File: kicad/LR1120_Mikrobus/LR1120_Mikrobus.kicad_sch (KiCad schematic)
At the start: 8 parts, among them IC1 BGA524N6E6327XTSA1, IC2 SKY13588-460LF, IC3 M24128-BFMH6TG, U1 LR1120, U4 LIS2DE12

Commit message: Small corrections from last commit
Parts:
- added U?: NT2016SA-40M-ENA4203A, symbol TCXO:NT2016SA-40M-ENA4203A
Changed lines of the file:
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@@
     (pin "9")
+  )
+  (symbol (lib_id "TCXO:NT2016SA-40M-ENA4203A") (at 57.15 66.04 0) (unit 1)
+    (in_bom yes) (on_board yes) (fields_autoplaced)
+    (property "Reference" "U?" (id 0) (at 58.42 53.34 0))
+    (property "Value" "NT2016SA-40M-ENA4203A" (id 1) (at 58.42 55.88 0))
+    (property "Footprint" "" (id 2) (at 57.15 66.04 0)
+      (effects (font (size 1.27 1.27)) hide)
+    )
+    (property "Datasheet" "" (id 3) (at 57.15 66.04 0)
+      (effects (font (size 1.27 1.27)) hide)
+    )
+    (pin "1")
+    (pin "2")
+    (pin "3")
+    (pin "4")
   )
   (symbol (lib_id "M24128-BFMH6TG:M24128-BFMH6TG") (at 233.68 85.09 0) (unit 1)
@@
       (reference "U4") (unit 1) (value "LIS2DE12") (footprint "Package_LGA:LGA-12_2x2mm_P0.5mm")
     )
+    (path "/ef4af352-5d7c-4ee8-a333-c7263e32c96e"
+      (reference "U?") (unit 1) (value "NT2016SA-40M-ENA4203A") (footprint "")
+    )
     (path "/30d9f59d-f72b-41c4-8214-d95fedfe532c"

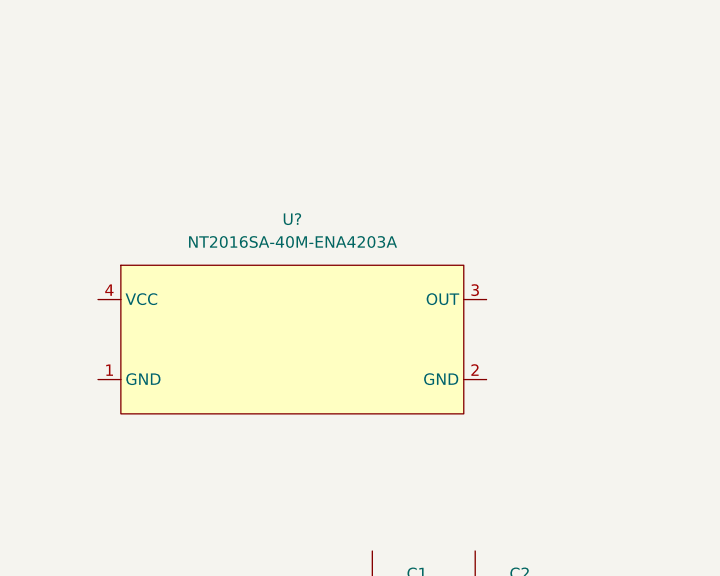
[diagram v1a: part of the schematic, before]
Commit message: tcxo footprint and symbol ready
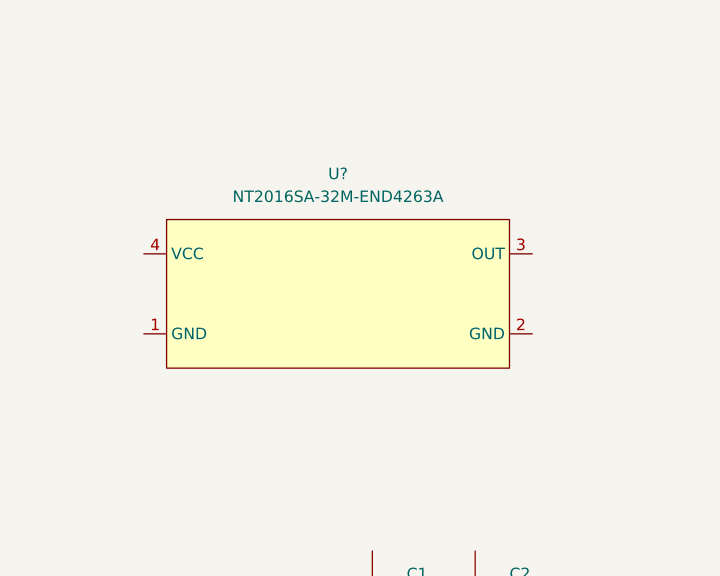
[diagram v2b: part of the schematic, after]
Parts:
- removed U?: NT2016SA-40M-ENA4203A, symbol TCXO:NT2016SA-40M-ENA4203A
- added U?: NT2016SA-32M-END4263A, TXCO:NT2016SA-32M-END4263A, symbol TCXO:NT2016SA-32M-END4263A
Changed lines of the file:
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@@
     (pin "9")
+  )
+  (symbol (lib_id "TCXO:NT2016SA-32M-END4263A") (at 62.23 60.96 0) (unit 1)
+    (in_bom yes) (on_board yes) (fields_autoplaced)
+    (property "Reference" "U?" (id 0) (at 63.5 48.26 0))
+    (property "Value" "NT2016SA-32M-END4263A" (id 1) (at 63.5 50.8 0))
+    (property "Footprint" "TXCO:NT2016SA-32M-END4263A" (id 2) (at 62.23 60.96 0)
+      (effects (font (size 1.27 1.27)) hide)
+    )
+    (property "Datasheet" "" (id 3) (at 62.23 60.96 0)
+      (effects (font (size 1.27 1.27)) hide)
+    )
+    (pin "1")
+    (pin "2")
+    (pin "3")
+    (pin "4")
   )
   (symbol (lib_id "Device:C") (at 67.31 93.98 0) (unit 1)
@@
     (pin "9")
   )
-  (symbol (lib_id "TCXO:NT2016SA-40M-ENA4203A") (at 57.15 66.04 0) (unit 1)
-    (in_bom yes) (on_board yes) (fields_autoplaced)
-    (property "Reference" "U?" (id 0) (at 58.42 53.34 0))
-    (property "Value" "NT2016SA-40M-ENA4203A" (id 1) (at 58.42 55.88 0))
-    (property "Footprint" "" (id 2) (at 57.15 66.04 0)
-      (effects (font (size 1.27 1.27)) hide)
-    )
-    (property "Datasheet" "" (id 3) (at 57.15 66.04 0)
-      (effects (font (size 1.27 1.27)) hide)
-    )
-    (pin "1")
-    (pin "2")
-    (pin "3")
-    (pin "4")
-  )
   (symbol (lib_id "M24128-BFMH6TG:M24128-BFMH6TG") (at 233.68 85.09 0) (unit 1)
     (in_bom yes) (on_board yes) (fields_autoplaced)
@@
       (reference "U4") (unit 1) (value "LIS2DE12") (footprint "Package_LGA:LGA-12_2x2mm_P0.5mm")
     )
-    (path "/ef4af352-5d7c-4ee8-a333-c7263e32c96e"
-      (reference "U?") (unit 1) (value "NT2016SA-40M-ENA4203A") (footprint "")
+    (path "/82107e2f-5ae3-45c6-a719-55de61f5c3b5"
+      (reference "U?") (unit 1) (value "NT2016SA-32M-END4263A") (footprint "TXCO:NT2016SA-32M-END4263A")
     )
     (path "/30d9f59d-f72b-41c4-8214-d95fedfe532c"

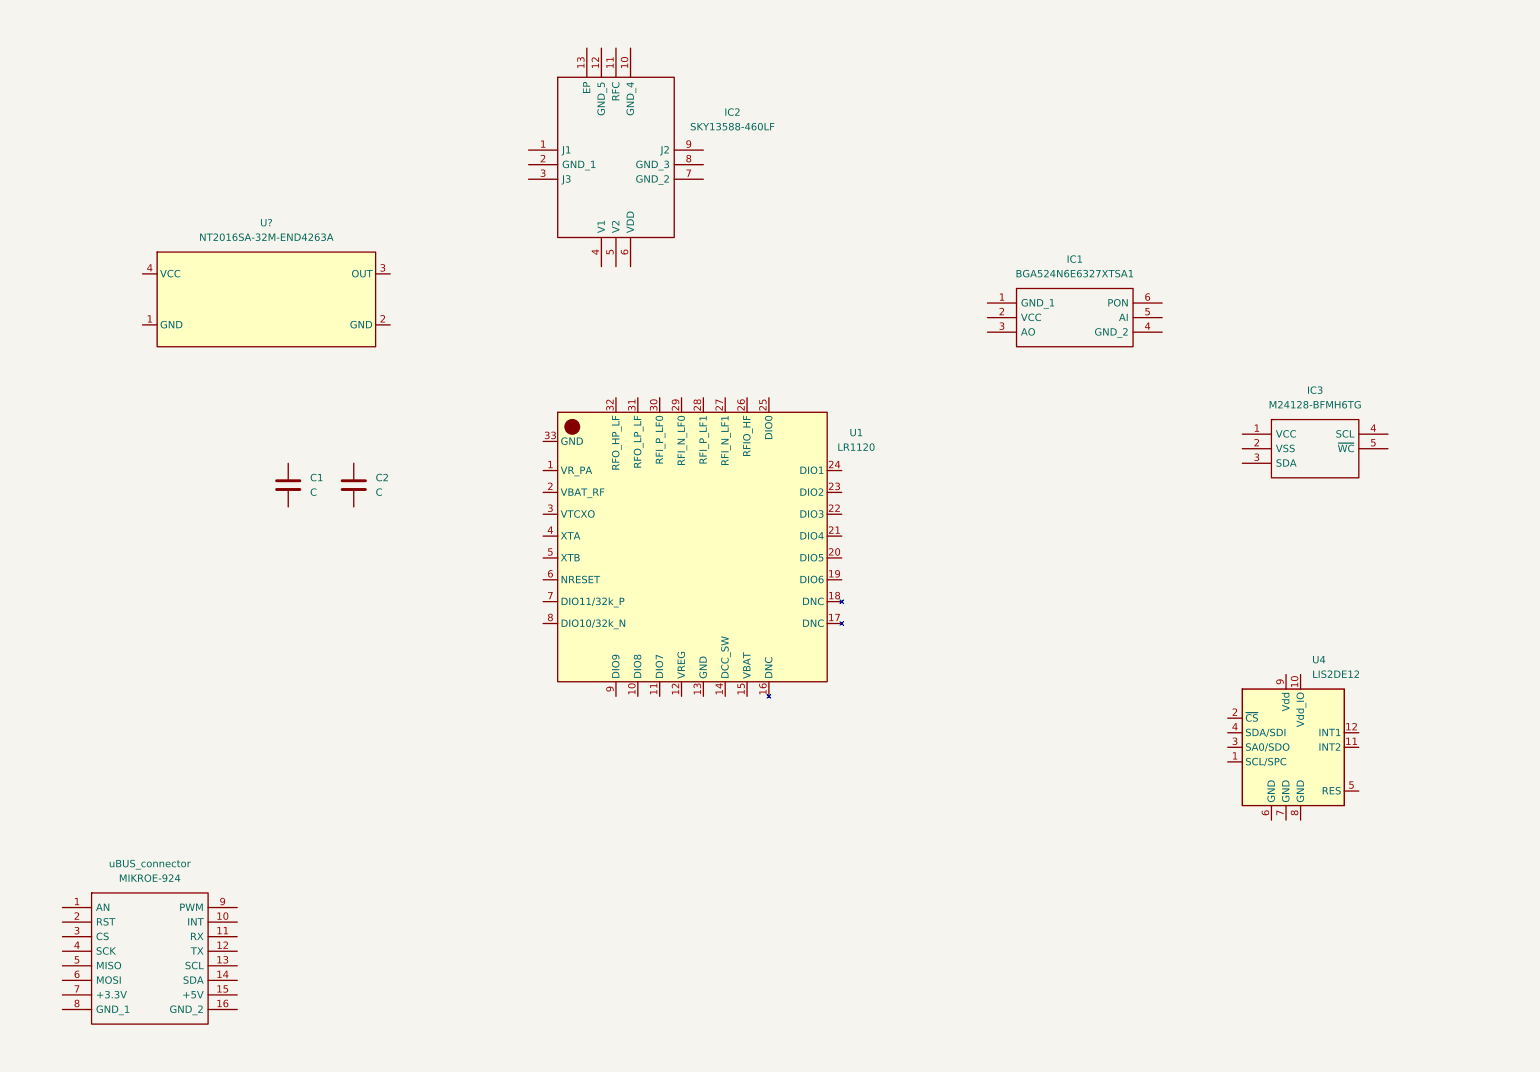
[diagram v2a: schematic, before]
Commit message: Q2 and Q3 placed
downloaded Q2 symbol and footprint. created Q3 symbol and footprint
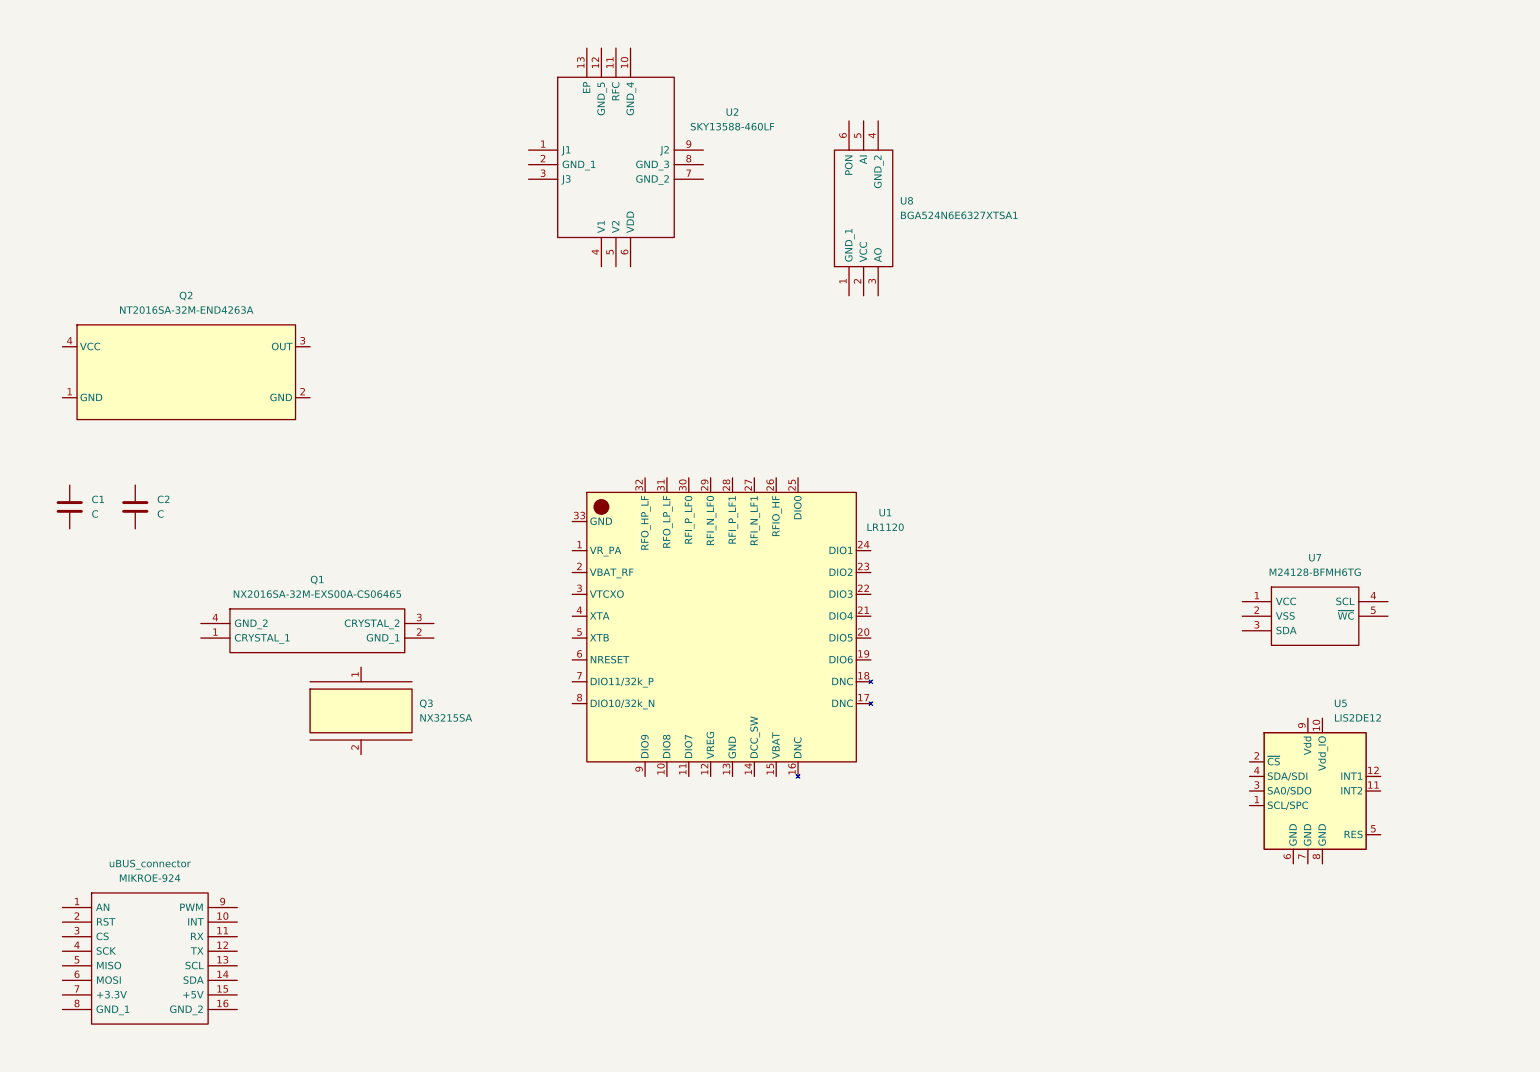
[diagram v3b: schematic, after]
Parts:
- added Q1: NX2016SA-32M-EXS00A-CS06465, EXS00A-CS06465:NX2016SA32MEXS00ACS06465, symbol NX2016SA-32M-EXS00A-CS06465:NX2016SA-32M-EXS00A-CS06465
- added Q3: NX3215SA, TXCO:NX3215SA, symbol TCXO:NX3215SA
- gave numbers to parts that had none: 1
- renumbered IC2 to U2, U4 to U5, IC3 to U7, IC1 to U8
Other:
- moved on the sheet: C1, C2, Q2, U1, U5, U7, U8

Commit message: added some res, ind and caps
added R9, R10, R17, R18 and R32. added C1-C7, C43-C46, C56 and C57. added L1.
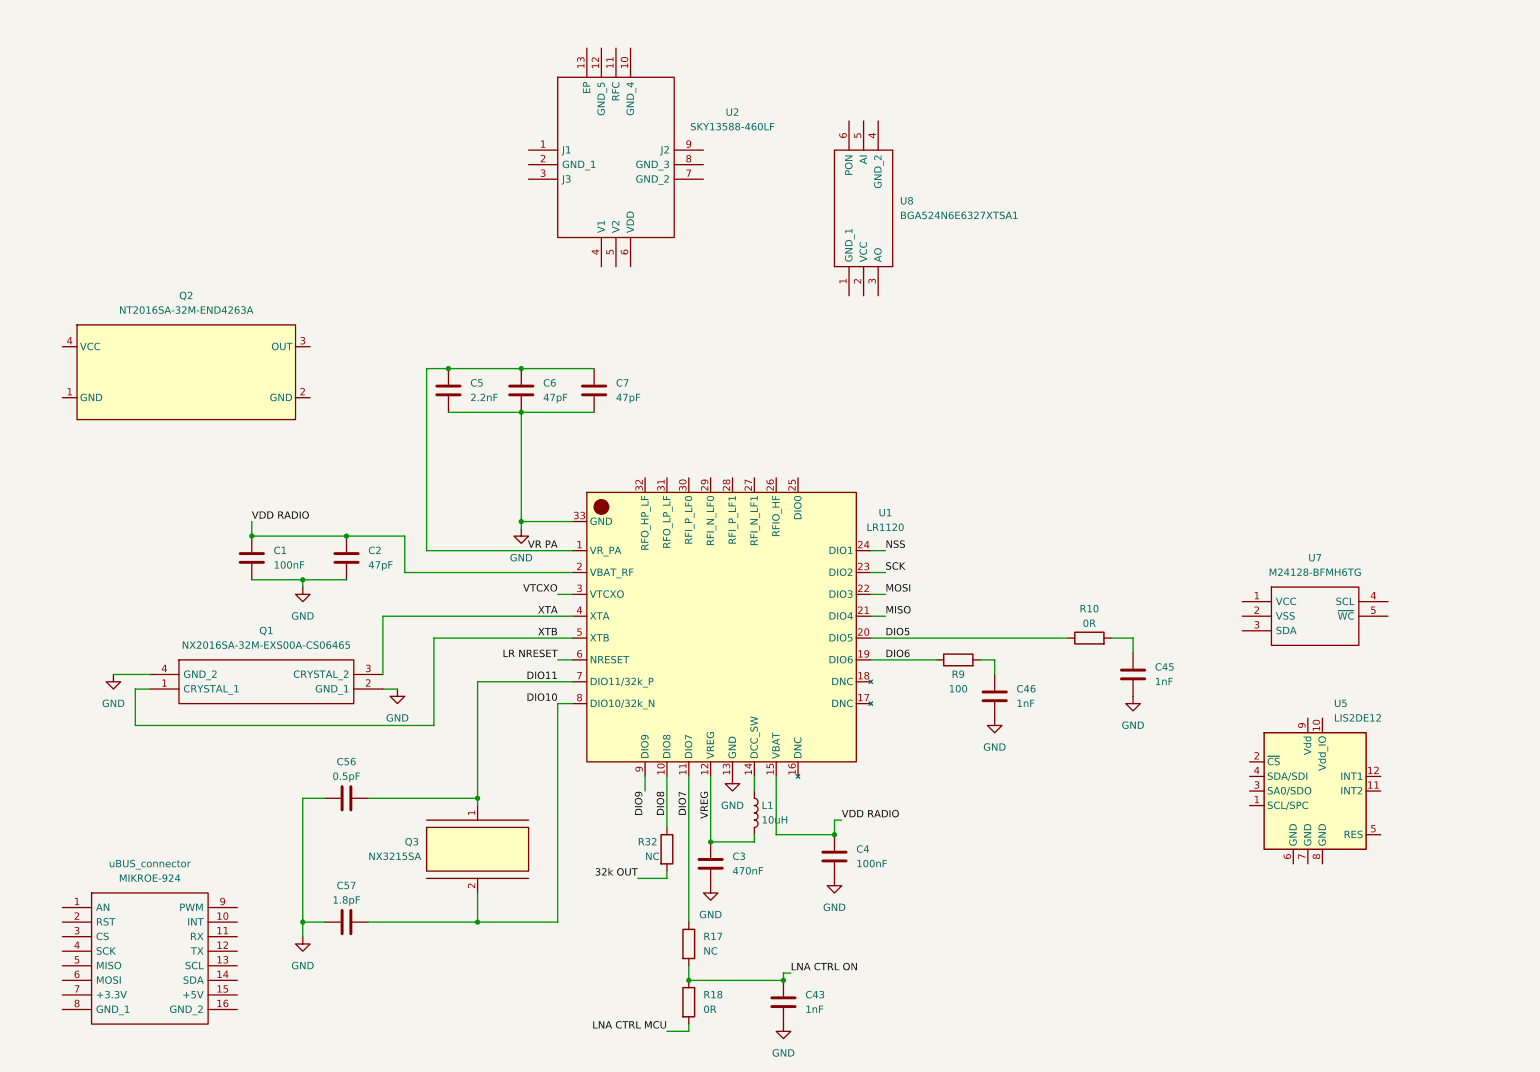
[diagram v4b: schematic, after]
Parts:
- added C3: 470nF, Capacitor_SMD:C_0201_0603Metric, symbol Device:C
- added C4: 100nF, Capacitor_SMD:C_0201_0603Metric, symbol Device:C
- added C43, C45, C46: 1nF, Capacitor_SMD:C_0201_0603Metric, symbol Device:C
- added C5: 2.2nF, Capacitor_SMD:C_0201_0603Metric, symbol Device:C
- added C56: 0.5pF, Capacitor_SMD:C_0201_0603Metric, symbol Device:C
- added C57: 1.8pF, Capacitor_SMD:C_0201_0603Metric, symbol Device:C
- added C6, C7: 47pF, Capacitor_SMD:C_0201_0603Metric, symbol Device:C
- added L1: 10uH, Inductor_SMD:L_0603_1608Metric, symbol Device:L
- added R10: 0R, Resistor_SMD:R_0603_1608Metric, symbol Device:R
- added R17, R32: NC, Resistor_SMD:R_0201_0603Metric, symbol Device:R
- added R18: 0R, Resistor_SMD:R_0201_0603Metric, symbol Device:R
- added R9: 100, Resistor_SMD:R_0201_0603Metric, symbol Device:R
- C1: value C -> 100nF; footprint (none) -> Capacitor_SMD:C_0201_0603Metric
- C2: value C -> 47pF; footprint (none) -> Capacitor_SMD:C_0201_0603Metric
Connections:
- net VDD RADIO: now reaches C2.1
- net VDD RADIO: now also C1.1, U1.15 (VBAT), U1.2 (VBAT_RF), C4.1
- net GND: now reaches C2.2
- net GND: now also C1.2, Q1.2 (GND_1), Q1.4 (GND_2), U1.13 (GND), U1.33 (GND), C3.2, C4.2, C43.2, C45.2, C46.2, C5.2, C56.1, C57.1, C6.2, C7.2
- net DIO11: now reaches Q3.1 (C1)
- net DIO11: now also U1.7 (DIO11/32k_P), C56.2
- net DIO10: now reaches Q3.2 (C2)
- net DIO10: now also U1.8 (DIO10/32k_N), C57.2
- net VR PA: now reaches U1.1 (VR_PA)
- net VR PA: now also C5.1, C6.1, C7.1
- net DIO8: now reaches U1.10 (DIO8)
- net DIO8: now also R32.1
- net DIO7: now reaches U1.11 (DIO7)
- net DIO7: now also R17.1
- net VREG: now reaches U1.12 (VREG)
- net VREG: now also C3.1, L1.2
- net at U1.14 (DCC_SW): now also L1.1
- net DIO6: now reaches U1.19 (DIO6)
- net DIO6: now also R9.1
- net DIO5: now reaches U1.20 (DIO5)
- net DIO5: now also R10.1
- net MISO: now reaches U1.21 (DIO4)
- net MOSI: now reaches U1.22 (DIO3)
- net SCK: now reaches U1.23 (DIO2)
- net NSS: now reaches U1.24 (DIO1)
- net VTCXO: now reaches U1.3 (VTCXO)
- net XTA: now reaches U1.4 (XTA)
- net XTA: now also Q1.3 (CRYSTAL_2)
- net XTB: now reaches U1.5 (XTB)
- net XTB: now also Q1.1 (CRYSTAL_1)
- net LR NRESET: now reaches U1.6 (NRESET)
- net DIO9: now reaches U1.9 (DIO9)
- new net: C46.1, R9.2
- new net: C45.1, R10.2
- new net 32k OUT: R32.2
- new net LNA CTRL MCU: R18.2
- new net LNA CTRL ON: C43.1, R17.2, R18.1
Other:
- moved on the sheet: C1, C2, Q1, Q3
